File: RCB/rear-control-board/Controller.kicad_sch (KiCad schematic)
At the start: 21 parts, among them J6 FTSH-107-01-F-DV-K, U1 STM32F413CGUx, U4 MAX33054EASA+T, Y1 CSTNE8M00

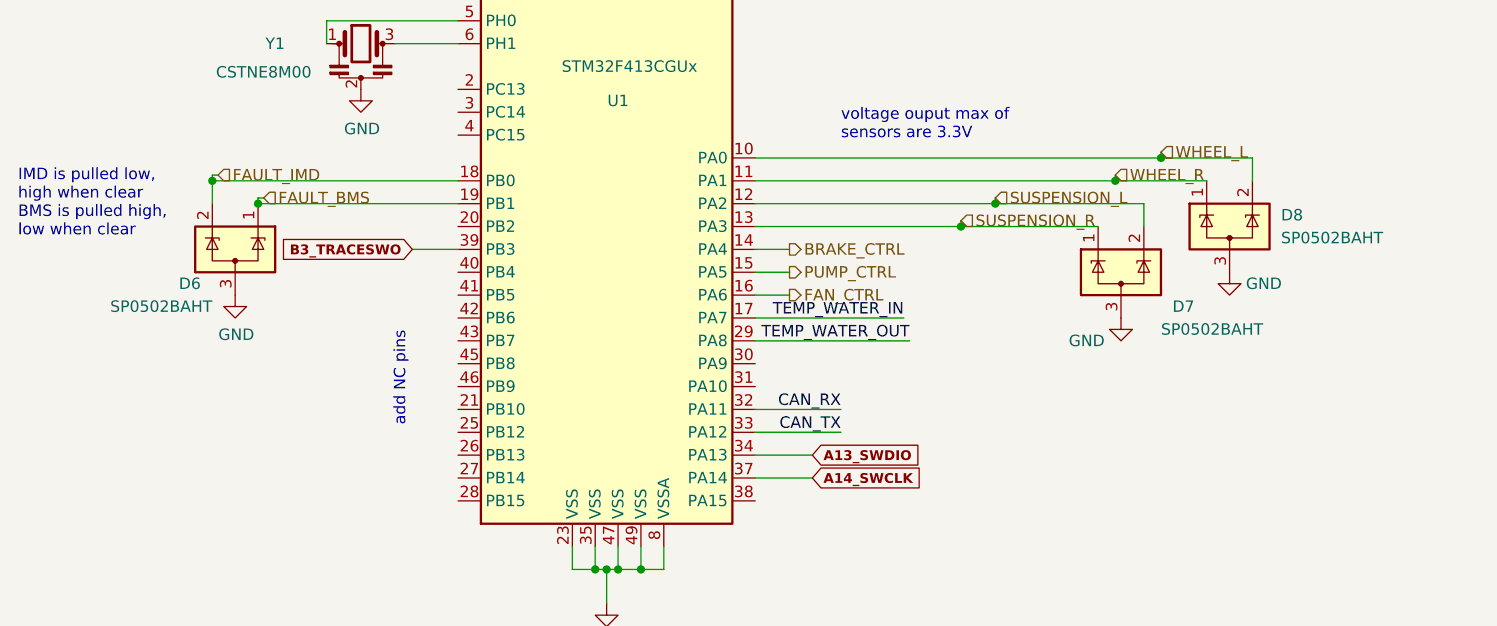
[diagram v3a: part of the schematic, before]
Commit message: updating layout with schem changes
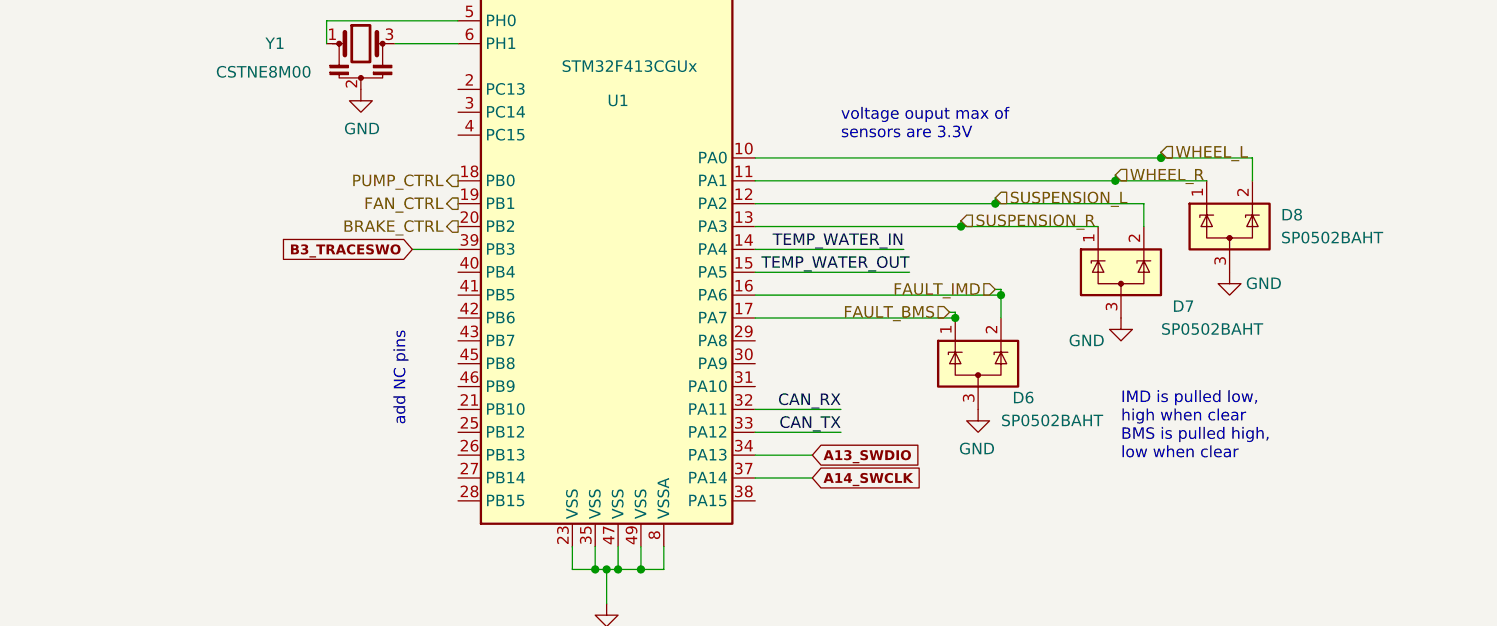
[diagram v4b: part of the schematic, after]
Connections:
- net BRAKE_CTRL: now also U1.20 (PB2); no longer U1.14 (PA4)
- net FAN_CTRL: now also U1.19 (PB1); no longer U1.16 (PA6)
- net FAULT_BMS: now also U1.17 (PA7); no longer U1.19 (PB1)
- net FAULT_IMD: now also U1.16 (PA6); no longer U1.18 (PB0)
- net PUMP_CTRL: now also U1.18 (PB0); no longer U1.15 (PA5)
- net WATER_IN-: now also U1.14 (PA4); no longer U1.17 (PA7)
- net WATER_OUT-: now also U1.15 (PA5); no longer U1.29 (PA8)
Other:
- moved on the sheet: D6
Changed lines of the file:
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@@
   (junction (at 136.525 146.05) (diameter 0) (color 0 0 0 0)
   )
-  (junction (at 36.195 146.05) (diameter 0) (color 0 0 0 0)
+  (junction (at 123.825 158.75) (diameter 0) (color 0 0 0 0)
   )
   (junction (at 81.28 102.87) (diameter 0) (color 0 0 0 0)
@@
   (junction (at 234.315 51.435) (diameter 0) (color 0 0 0 0)
   )
-  (junction (at 41.275 148.59) (diameter 0) (color 0 0 0 0)
+  (junction (at 118.745 161.29) (diameter 0) (color 0 0 0 0)
   )
   (junction (at 80.01 189.23) (diameter 0) (color 0 0 0 0)
@@
     (stroke (width 0) (type default) (color 0 0 0 0))
   )
-  (wire (pts (xy 41.275 148.59) (xy 63.5 148.59))
+  (wire (pts (xy 118.745 161.29) (xy 96.52 161.29))
     (stroke (width 0) (type default) (color 0 0 0 0))
   )
@@
     (stroke (width 0) (type default) (color 0 0 0 0))
   )
-  (wire (pts (xy 36.195 145.415) (xy 36.195 146.05))
-    (stroke (width 0) (type default) (color 0 0 0 0))
-  )
-  (wire (pts (xy 100.33 153.67) (xy 96.52 153.67))
+  (wire (pts (xy 123.825 158.115) (xy 123.825 158.75))
     (stroke (width 0) (type default) (color 0 0 0 0))
   )
@@
     (stroke (width 0) (type default) (color 0 0 0 0))
   )
-  (wire (pts (xy 36.83 145.415) (xy 36.195 145.415))
+  (wire (pts (xy 123.19 158.115) (xy 123.825 158.115))
     (stroke (width 0) (type default) (color 0 0 0 0))
   )
@@
     (stroke (width 0) (type default) (color 0 0 0 0))
   )
-  (wire (pts (xy 41.91 147.955) (xy 41.275 147.955))
+  (wire (pts (xy 118.11 160.655) (xy 118.745 160.655))
     (stroke (width 0) (type default) (color 0 0 0 0))
   )
@@
     (stroke (width 0) (type default) (color 0 0 0 0))
   )
-  (wire (pts (xy 96.52 163.83) (xy 113.665 163.83))
+  (wire (pts (xy 96.52 156.21) (xy 113.665 156.21))
     (stroke (width 0) (type default) (color 0 0 0 0))
   )
@@
     (stroke (width 0) (type default) (color 0 0 0 0))
   )
-  (wire (pts (xy 36.195 146.05) (xy 63.5 146.05))
+  (wire (pts (xy 123.825 158.75) (xy 96.52 158.75))
     (stroke (width 0) (type default) (color 0 0 0 0))
   )
@@
     (stroke (width 0) (type default) (color 0 0 0 0))
   )
-  (wire (pts (xy 100.33 156.21) (xy 96.52 156.21))
-    (stroke (width 0) (type default) (color 0 0 0 0))
-  )
   (wire (pts (xy 248.92 135.255) (xy 248.92 136.525))
     (stroke (width 0) (type default) (color 0 0 0 0))
   )
-  (wire (pts (xy 36.195 146.05) (xy 36.195 148.59))
-    (stroke (width 0) (type default) (color 0 0 0 0))
-  )
-  (wire (pts (xy 100.33 158.75) (xy 96.52 158.75))
+  (wire (pts (xy 123.825 158.75) (xy 123.825 161.29))
     (stroke (width 0) (type default) (color 0 0 0 0))
   )
@@
     (stroke (width 0) (type default) (color 0 0 0 0))
   )
-  (wire (pts (xy 41.275 147.955) (xy 41.275 148.59))
+  (wire (pts (xy 118.745 160.655) (xy 118.745 161.29))
     (stroke (width 0) (type default) (color 0 0 0 0))
   )
@@
     (stroke (width 0) (type default) (color 0 0 0 0))
   )
-  (wire (pts (xy 96.52 161.29) (xy 113.03 161.29))
+  (wire (pts (xy 96.52 153.67) (xy 113.03 153.67))
     (stroke (width 0) (type default) (color 0 0 0 0))
   )
@@
   )
   (text "IMD is pulled low, \nhigh when clear\nBMS is pulled high, \nlow when clear"
-    (at 14.605 152.4 0)
+    (at 137.16 177.165 0)
     (effects (font (size 1.27 1.27)) (justify left bottom))
   )
@@
     (effects (font (size 1.27 1.27)) (justify right bottom))
   )
-  (label "TEMP_WATER_OUT" (at 113.665 163.83 180)
+  (label "TEMP_WATER_OUT" (at 113.665 156.21 180)
     (effects (font (size 1.27 1.27)) (justify right bottom))
   )
@@
     (effects (font (size 1.27 1.27)) (justify right bottom))
   )
-  (label "TEMP_WATER_IN" (at 113.03 161.29 180)
+  (label "TEMP_WATER_IN" (at 113.03 153.67 180)
     (effects (font (size 1.27 1.27)) (justify right bottom))
   )
@@
     )
   )
-  (hierarchical_label "FAN_CTRL" (shape output) (at 100.33 158.75 0)
-    (effects (font (size 1.27 1.27)) (justify left))
+  (hierarchical_label "FAN_CTRL" (shape output) (at 63.5 148.59 180)
+    (effects (font (size 1.27 1.27)) (justify right))
   )
   (hierarchical_label "SUSPENSION_L" (shape input) (at 123.19 147.955 0)
@@
     (effects (font (size 1.27 1.27)) (justify right))
   )
-  (hierarchical_label "PUMP_CTRL" (shape output) (at 100.33 156.21 0)
-    (effects (font (size 1.27 1.27)) (justify left))
+  (hierarchical_label "PUMP_CTRL" (shape output) (at 63.5 146.05 180)
+    (effects (font (size 1.27 1.27)) (justify right))
   )
   (hierarchical_label "CAN_N" (shape output) (at 253.365 142.875 0)
@@
     (effects (font (size 1.27 1.27)) (justify left))
   )
-  (hierarchical_label "BRAKE_CTRL" (shape output) (at 100.33 153.67 0)
-    (effects (font (size 1.27 1.27)) (justify left))
-  )
-  (hierarchical_label "FAULT_IMD" (shape input) (at 36.83 145.415 0)
-    (effects (font (size 1.27 1.27)) (justify left))
+  (hierarchical_label "BRAKE_CTRL" (shape output) (at 63.5 151.13 180)
+    (effects (font (size 1.27 1.27)) (justify right))
+  )
+  (hierarchical_label "FAULT_IMD" (shape input) (at 123.19 158.115 180)
+    (effects (font (size 1.27 1.27)) (justify right))
   )
   (hierarchical_label "WATER_IN+" (shape input) (at 137.795 27.305 180)
@@
     (effects (font (size 1.27 1.27)) (justify left))
   )
-  (hierarchical_label "FAULT_BMS" (shape input) (at 41.91 147.955 0)
-    (effects (font (size 1.27 1.27)) (justify left))
+  (hierarchical_label "FAULT_BMS" (shape input) (at 118.11 160.655 180)
+    (effects (font (size 1.27 1.27)) (justify right))
   )
   (symbol (lib_id "MCU_ST_STM32F4:STM32F413CGUx") (at 81.28 146.05 0) (unit 1)
@@
     (pin "2")
   )
-  (symbol (lib_id "Power_Protection:SP0502BAHT") (at 38.735 153.67 0) (mirror y) (unit 1)
-    (in_bom yes) (on_board yes)
-    (property "Reference" "D6" (id 0) (at 34.925 157.48 0)
-      (effects (font (size 1.27 1.27)) (justify left))
-    )
-    (property "Value" "SP0502BAHT" (id 1) (at 36.195 160.02 0)
-      (effects (font (size 1.27 1.27)) (justify left))
-    )
-    (property "Footprint" "Package_TO_SOT_SMD:SOT-23" (id 2) (at 33.02 154.94 0)
+  (symbol (lib_id "Power_Protection:SP0502BAHT") (at 121.285 166.37 0) (unit 1)
+    (in_bom yes) (on_board yes)
+    (property "Reference" "D6" (id 0) (at 125.095 170.18 0)
+      (effects (font (size 1.27 1.27)) (justify left))
+    )
+    (property "Value" "SP0502BAHT" (id 1) (at 123.825 172.72 0)
+      (effects (font (size 1.27 1.27)) (justify left))
+    )
+    (property "Footprint" "Package_TO_SOT_SMD:SOT-23" (id 2) (at 127 167.64 0)
       (effects (font (size 1.27 1.27)) (justify left) hide)
     )
-    (property "Datasheet" "http://www.littelfuse.com/~/media/files/littelfuse/technical%20resources/documents/data%20sheets/sp05xxba.pdf" (id 3) (at 35.56 150.495 0)
+    (property "Datasheet" "http://www.littelfuse.com/~/media/files/littelfuse/technical%20resources/documents/data%20sheets/sp05xxba.pdf" (id 3) (at 124.46 163.195 0)
       (effects (font (size 1.27 1.27)) hide)
     )
@@
     (pin "9")
   )
-  (symbol (lib_id "power:GND") (at 38.735 158.75 0) (unit 1)
-    (in_bom yes) (on_board yes)
-    (property "Reference" "#PWR0111" (id 0) (at 38.735 165.1 0)
-      (effects (font (size 1.27 1.27)) hide)
-    )
-    (property "Value" "GND" (id 1) (at 38.862 163.1442 0))
-    (property "Footprint" "" (id 2) (at 38.735 158.75 0)
-      (effects (font (size 1.27 1.27)) hide)
-    )
-    (property "Datasheet" "" (id 3) (at 38.735 158.75 0)
-      (effects (font (size 1.27 1.27)) hide)
-    )
+  (symbol (lib_id "power:GND") (at 121.285 171.45 0) (mirror y) (unit 1)
+    (in_bom yes) (on_board yes)
+    (property "Reference" "#PWR0111" (id 0) (at 121.285 177.8 0)
+      (effects (font (size 1.27 1.27)) hide)
+    )
+    (property "Value" "GND" (id 1) (at 121.158 175.8442 0))
+    (property "Footprint" "" (id 2) (at 121.285 171.45 0)
+      (effects (font (size 1.27 1.27)) hide)
+    )
+    (property "Datasheet" "" (id 3) (at 121.285 171.45 0)
+      (effects (font (size 1.27 1.27)) hide)
+    )

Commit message: Addded comments
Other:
- note added: "DNP"
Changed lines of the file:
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@@
     (effects (font (size 1.27 1.27)) (justify left bottom))
+  )
+  (text "DNP\n" (at 252.73 140.97 0)
+    (effects (font (size 1.27 1.27) bold italic) (justify left bottom))
   )
   (text "STBY logic low is normal mode\nlogic high is receive only"
